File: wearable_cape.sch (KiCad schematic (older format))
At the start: 72 parts, among them J1 JACK_3P, J2 JACK_3P, J3 JACK_3P, P1 BELA_AINS, P2 RECEIVER, P3 BATTERY, P4 BELA_AOUTS, P5 PWR_OUT, SW1 SW_HALT, SW2 SW_MODE_SEL, U1 MCP6004, U2 MCP6004, U3 BEAGLEBONEBLACK, U4 OKI_7805

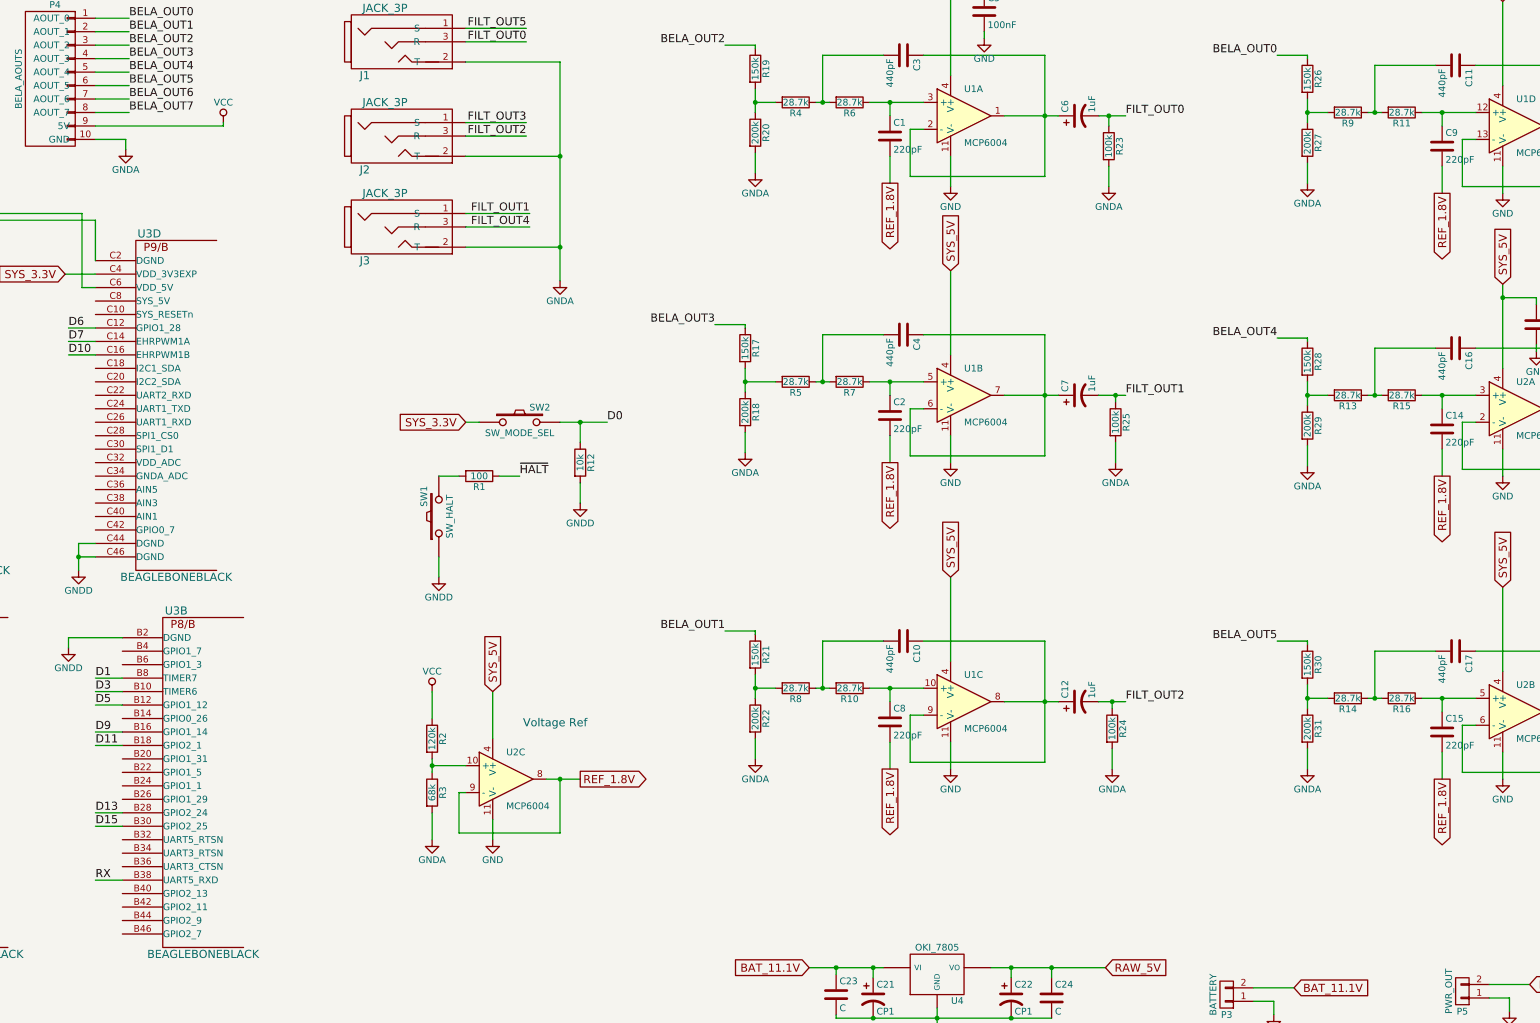
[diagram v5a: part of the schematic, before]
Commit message: add ferrite beads, and fix GNDA -> 1.8_VREF
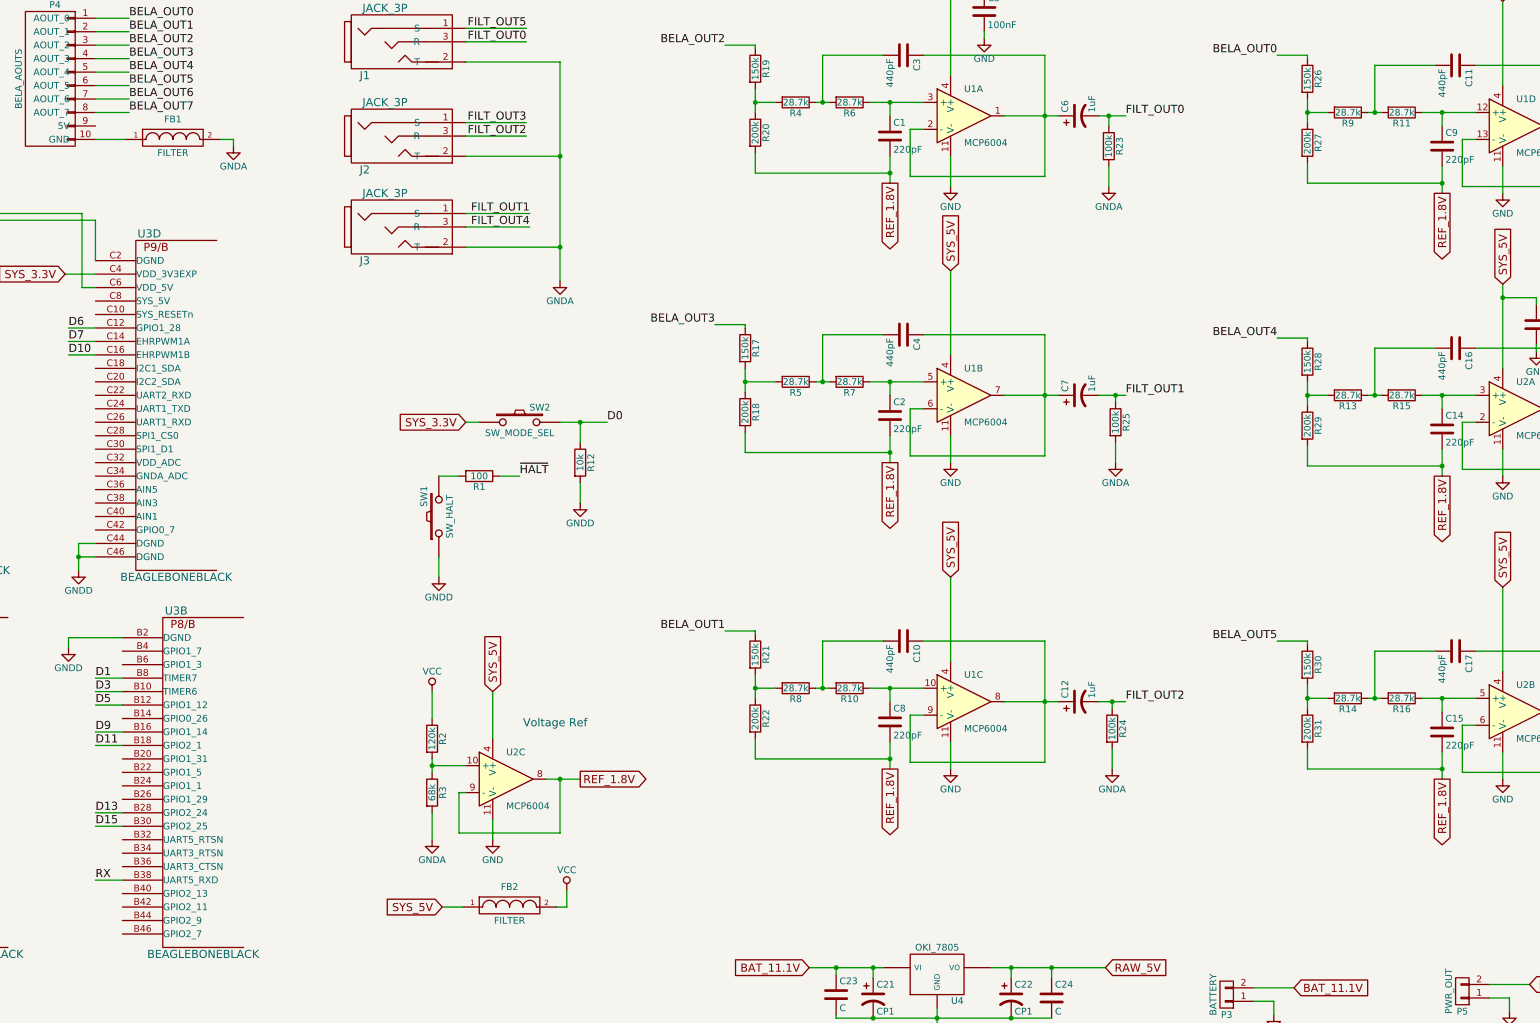
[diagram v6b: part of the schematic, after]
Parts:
- added FB1, FB2: FILTER, Resistors_SMD:R_0603_HandSoldering, symbol FILTER
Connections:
- net GNDA: now also FB1.2; no longer P4.10 (GND), R18.2, R20.2, R22.2, R27.2, R29.2, R31.2
- net REF_1.8V: now also R18.2, R20.2, R22.2, R27.2, R29.2, R31.2
- net SYS_5V: now also FB2.1
- net VCC: now also FB2.2; no longer P4.9 (5V)
- new net: FB1.1, P4.10 (GND)

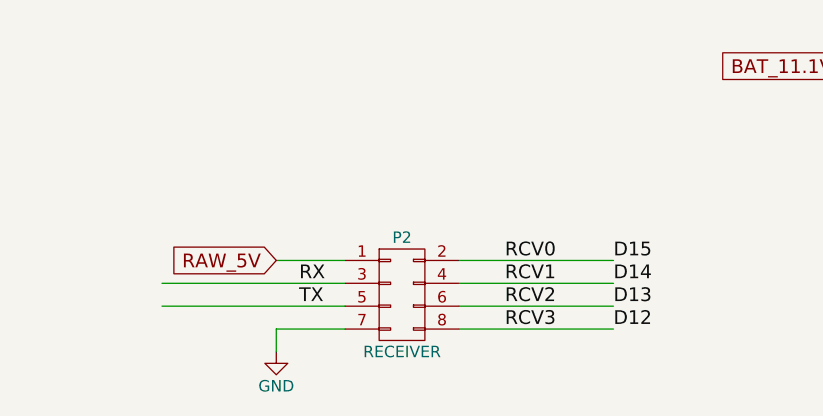
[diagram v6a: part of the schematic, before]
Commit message: updates: footprint check, cutout for regulator, larger power input screw terminal
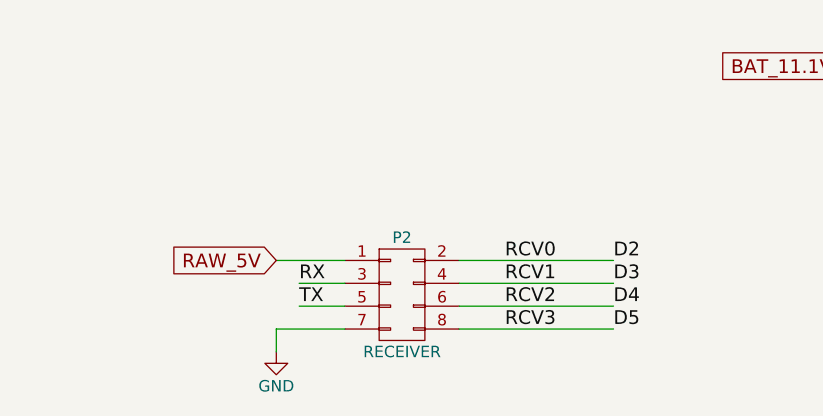
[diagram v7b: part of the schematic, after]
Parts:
- P2: footprint Socket_Strips:Socket_Strip_Straight_2x04 -> IDC_header_8pin:IDC_Header_Straight_10pins
- P3: footprint Terminal_Blocks:TerminalBlock_Pheonix_MPT-2.54mm_2pol -> Terminal_Blocks:TerminalBlock_Pheonix_PT-3.5mm_2pol
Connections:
- net D12: no longer P2.8 (P8)
- net D13: no longer P2.6 (P6)
- net D14: no longer P2.4 (P4)
- net D15: no longer P2.2 (P2)
- net D2: now also P2.2 (P2)
- net D3: now also P2.4 (P4)
- net D4: now also P2.6 (P6)
- net D5: now also P2.8 (P8)
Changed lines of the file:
@@
 F 0 "P2" H 7100 9300 50  0000 C CNN
 F 1 "RECEIVER" H 7100 8800 50  0000 C CNN
-F 2 "Socket_Strips:Socket_Strip_Straight_2x04" H 7100 7850 50  0001 C CNN
+F 2 "IDC_header_8pin:IDC_Header_Straight_10pins" H 7100 7850 50  0001 C CNN
 F 3 "" H 7100 7850 50  0000 C CNN
 	1    7100 9050
@@
 Text GLabel 6550 8900 0    60   Input ~ 0
 RAW_5V
-Wire Wire Line
-	6050 9000 6850 9000
-Wire Wire Line
-	6050 9100 6850 9100
 Text Label 6650 9000 0    60   ~ 0
 RX
@@
 F 0 "P3" H 12150 8400 50  0000 C CNN
 F 1 "BATTERY" V 12250 8250 50  0000 C CNN
-F 2 "Terminal_Blocks:TerminalBlock_Pheonix_MPT-2.54mm_2pol" H 12150 8250 50  0001 C CNN
+F 2 "Terminal_Blocks:TerminalBlock_Pheonix_PT-3.5mm_2pol" H 12150 8250 50  0001 C CNN
 F 3 "" H 12150 8250 50  0000 C CNN
 	1    12150 8250
@@
 	1750 2575 2000 2575
 Connection ~ 2000 2575
+Text Label 8025 8900 0    60   ~ 0
+D2
+Text Label 8025 9000 0    60   ~ 0
+D3
+Text Label 8025 9100 0    60   ~ 0
+D4
 Text Label 8025 9200 0    60   ~ 0
-D12
-Text Label 8025 9100 0    60   ~ 0
-D13
-Text Label 8025 9000 0    60   ~ 0
-D14
-Text Label 8025 8900 0    60   ~ 0
-D15
+D5
 Wire Wire Line
 	2200 7400 1925 7400
@@
 Wire Wire Line
 	4775 1900 4675 1900
+Wire Wire Line
+	6650 9000 6850 9000
+Wire Wire Line
+	6850 9100 6650 9100
 $EndSCHEMATC

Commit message: added several options for attenuation of circuit.
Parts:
- added R35, R36, R37, R38, R39, R40: 12k, Resistors_SMD:R_0603_HandSoldering, symbol R
- R17, R19, R21, R26, R28, R30: value 150k -> 2k2
- R18, R20, R22, R27, R29, R31: value 200k -> 390
- R23, R24, R25, R32, R33, R34: value 100k -> 3k9
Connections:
- net BELA_OUT0: now also R27.1, R9.2; no longer R26.1
- net BELA_OUT1: now also R22.1, R8.2; no longer R21.1
- net BELA_OUT2: now also R20.1, R4.2; no longer R19.1
- net BELA_OUT3: now also R18.1, R5.2; no longer R17.1
- net BELA_OUT4: now also R13.2, R29.1; no longer R28.1
- net BELA_OUT5: now also R14.2, R31.1; no longer R30.1
- net FILT_OUT0: now also R37.1; no longer C6.2, R23.1
- net FILT_OUT1: now also R36.1; no longer C7.2, R25.1
- net FILT_OUT2: now also R35.1; no longer C12.2, R24.1
- net FILT_OUT3: now also R38.1; no longer C13.2, R33.1
- net FILT_OUT4: now also R39.1; no longer C18.2, R32.1
- net FILT_OUT5: now also R40.1; no longer C19.2, R34.1
- net GNDA: now also R18.2, R20.2, R22.2, R27.2, R29.2, R31.2
- net REF_1.8V: no longer R18.2, R20.2, R22.2, R27.2, R29.2, R31.2
- new net: C7.2, R19.2
- new net: C6.2, R21.2
- new net: C13.2, R26.2
- new net: C12.2, R17.1
- new net: C18.2, R30.2
- new net: C19.2, R28.2
- new net: R21.1, R23.1, R37.2
- new net: R19.1, R25.1, R36.2
- new net: R17.2, R24.1, R35.2
- new net: R26.1, R32.1, R38.2
- new net: R30.1, R34.1, R39.2
- new net: R28.1, R33.1, R40.2
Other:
- moved on the sheet: C1, C10, C11, C12, C13, C14, C15, C16, C17, C18, C19, C2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
